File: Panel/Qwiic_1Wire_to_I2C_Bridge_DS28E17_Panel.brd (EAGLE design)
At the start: 45.7 x 27.9 mm, 23 parts, among them J1 RJ45, J2 RJ45, J3 RJ11, J4 RJ11, U1 DS28E17

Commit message: Update to board
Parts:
- removed FRAME1: FRAME-LETTER, SparkFun-Aesthetics:CREATIVE_COMMONS
- added C2: 1.0uF, SparkFun-Capacitors:0603
- added H5, H6, H7, H8: STAND-OFF, SparkFun-Hardware:STAND-OFF
- added J10: (no value), SparkFun-Connectors:1X03
- added J6, J8: RJ45, SparkFun-Connectors:RJ45-8
- added J7, J9: RJ11, SparkFun-Connectors:RJ11-6
- added JP10: (no value), SparkFun-Jumpers:SMT-JUMPER_3_2-NC_PASTE_SILK
- added JP4, JP7: (no value), SparkX:1X04_1MM_RA
- added JP8: (no value), SparkX:1X04
- added JP9: (no value), SparkFun-Jumpers:SMT-JUMPER_2_NC_PASTE_SILK
- added LOGO2: OSHW-LOGOM, SparkFun-Aesthetics:OSHW-LOGO-M
- added R4, R5, R6: 4.7k, SparkFun-Resistors:0603
- added U$1, U$4: SPARKX-LOGO5, SparkX:SPARKX-LARGE
- added U2: DS28E17, SparkX:TQFN-16
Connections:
- new net 3.3V1: J10.3, J6.6, J7.5, J8.6, J9.5, JP10.2, JP4.2, JP7.2, JP8.2, JP9.2, U2.6
- new net AWAKE1: U2.12
- new net BUSY1: U2.13
- new net ED1: U2.5
- new net GND1: C2.2, J10.1, J6.4, J7.3, J8.4, J9.3, JP4.1, JP7.1, JP8.1, U2.4, U2.8
- new net IO1: J10.2, J6.5, J7.4, J8.5, J9.4, R6.1, U2.2, U2.3
- new net N$5: C2.1, U2.7
- new net N$6: JP9.1, R6.2
- new net N$7: JP10.1, R5.2
- new net N$8: JP10.3, R4.2
- new net SCL1: JP4.4, JP7.4, JP8.4, R4.1, U2.15
- new net SDA1: JP4.3, JP7.3, JP8.3, R5.1, U2.16
- new net XD1: U2.14
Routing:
- net 3.3V1: track 0.00 -> 82.0 mm, vias 0 -> 1
- net IO1: track 0.00 -> 48.5 mm
- net SCL1: track 0.00 -> 37.8 mm, vias 0 -> 3
- net SDA1: track 0.00 -> 36.5 mm, vias 0 -> 3
- net N$5: track 0.00 -> 3.68 mm
- net N$6: track 0.00 -> 3.11 mm
- net N$8: track 0.00 -> 2.56 mm
- net N$7: track 0.00 -> 2.56 mm
- added copper zone on layer 1, net GND1
- added copper zone on layer 16, net GND1
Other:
- board size 45.7 x 27.9 mm -> 91.9 x 27.9 mm
- board text removed: "Joel Bartlett"

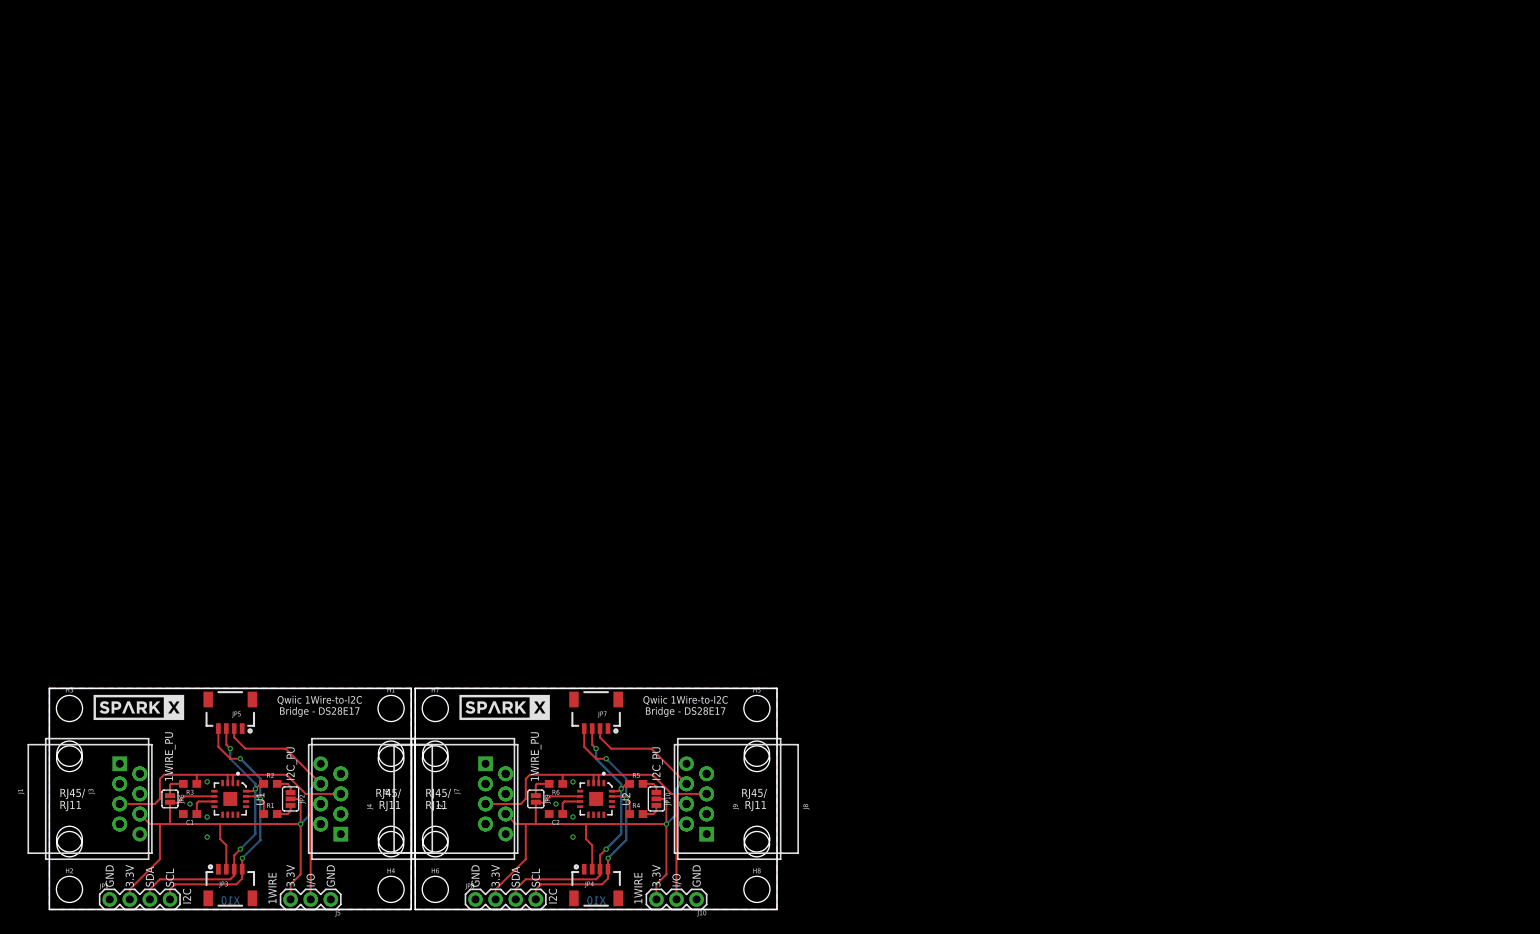
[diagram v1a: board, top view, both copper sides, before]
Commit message: Added RJ45/RJ11 footprint. CAM new panel gerbers
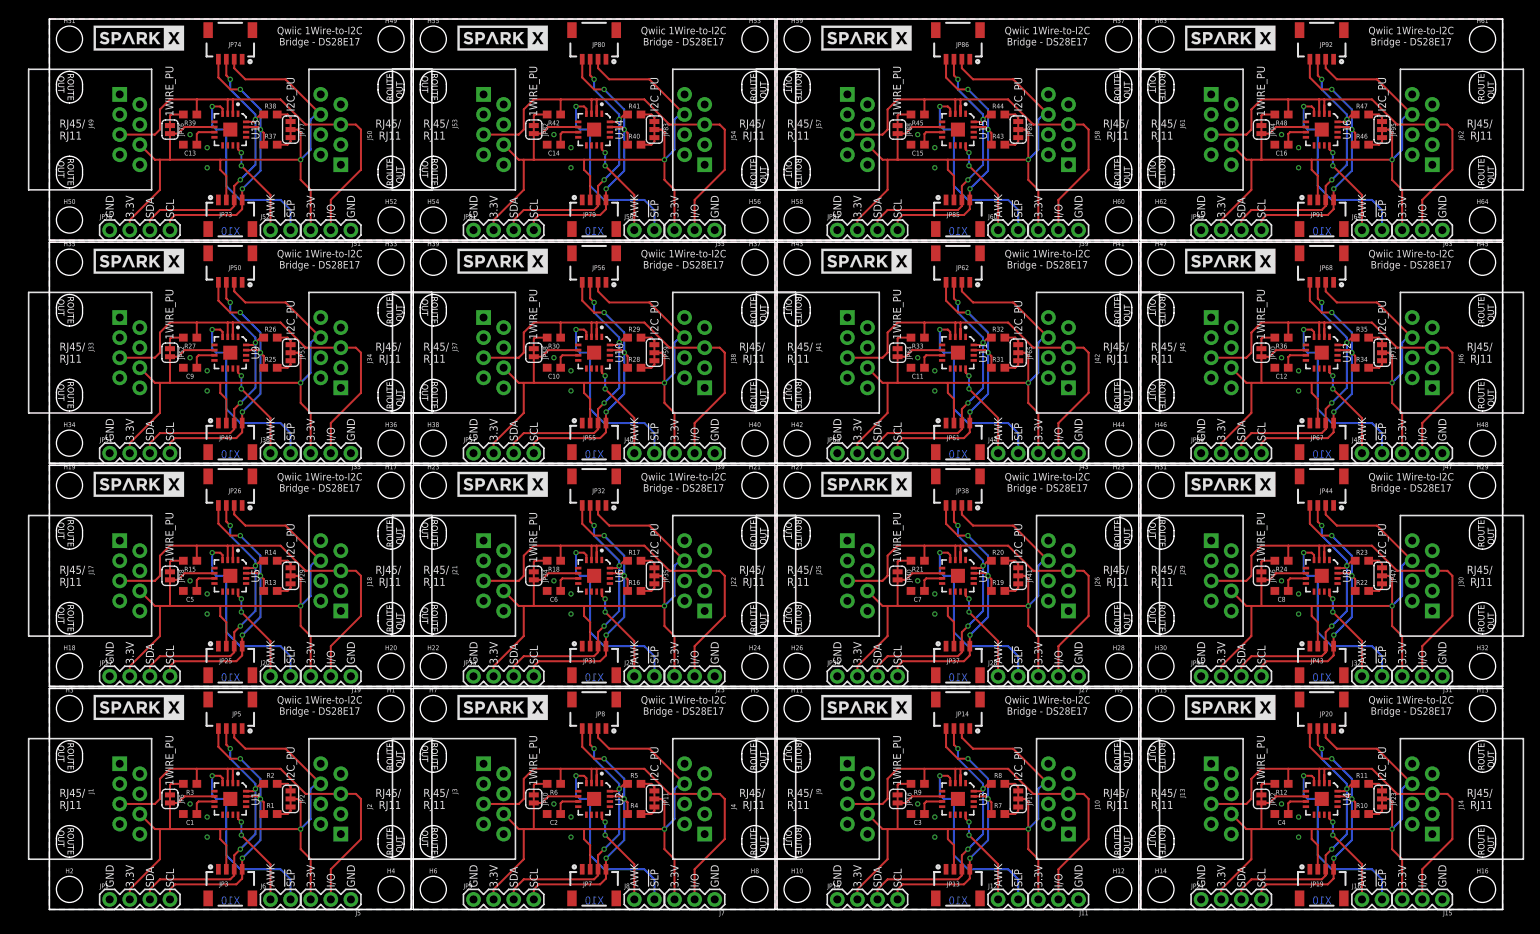
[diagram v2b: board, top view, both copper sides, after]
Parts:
- added C10, C11, C12, C13, C14, C15, C16, C3, C4, C5, C6, C7, C8, C9: 1.0uF, SparkFun-Capacitors:0603
- added FRAME1: FRAME-LETTER, SparkFun-Aesthetics:CREATIVE_COMMONS
- added H10, H11, H12, H13, H14, H15, H16, H17, H18, H19, H20, H21, H22, H23, H24, H25, H26, H27, H28, H29, H30, H31, H32, H33, H34, H35, H36, H37, H38, H39, H40, H41, H42, H43, H44, H45, H46, H47, H48, H49, H50, H51, H52, H53, H54, H55, H56, H57, H58, H59, H60, H61, H62, H63, H64, H9: STAND-OFF, SparkFun-Hardware:STAND-OFF
- added J11, J15, J19, J23, J27, J31, J35, J39, J43, J47, J51, J55, J59, J63: (no value), SparkFun-Connectors:1X03
- added J12, J16, J20, J24, J28, J32, J36, J40, J44, J48, J52, J56, J60, J64: (no value), SparkFun-Connectors:1X02
- added J13, J14, J17, J18, J21, J22, J25, J26, J29, J30, J33, J34, J37, J38, J41, J42, J45, J46, J49, J50, J53, J54, J57, J58, J61, J62: RJ45_RJ11_COMBO, SparkX:RJ45_RJ11_COMBO
- added JP11, JP17, JP23, JP29, JP35, JP41, JP47, JP53, JP59, JP65, JP71, JP77, JP83, JP89, JP95: (no value), SparkFun-Jumpers:SMT-JUMPER_3_2-NC_TRACE_SILK
- added JP12, JP16, JP18, JP22, JP24, JP28, JP30, JP34, JP36, JP40, JP42, JP46, JP48, JP52, JP54, JP58, JP60, JP64, JP66, JP70, JP72, JP76, JP78, JP82, JP84, JP88, JP90, JP94, JP96: (no value), SparkFun-Jumpers:SMT-JUMPER_2_NC_TRACE_SILK
- added JP13, JP14, JP19, JP20, JP25, JP26, JP31, JP32, JP37, JP38, JP43, JP44, JP49, JP50, JP55, JP56, JP61, JP62, JP67, JP68, JP73, JP74, JP79, JP80, JP85, JP86, JP91, JP92: (no value), SparkX:1X04_1MM_RA
- added JP15, JP21, JP27, JP33, JP39, JP45, JP51, JP57, JP63, JP69, JP75, JP81, JP87, JP93: (no value), SparkX:1X04
- added LOGO10, LOGO11, LOGO12, LOGO13, LOGO14, LOGO15, LOGO16, LOGO3, LOGO4, LOGO5, LOGO6, LOGO7, LOGO8, LOGO9: OSHW-LOGOM, SparkFun-Aesthetics:OSHW-LOGO-M
- added R10, R11, R12, R13, R14, R15, R16, R17, R18, R19, R20, R21, R22, R23, R24, R25, R26, R27, R28, R29, R30, R31, R32, R33, R34, R35, R36, R37, R38, R39, R40, R41, R42, R43, R44, R45, R46, R47, R48, R7, R8, R9: 4.7k, SparkFun-Resistors:0603
- added U$10, U$11, U$12, U$13, U$14, U$15, U$16, U$17, U$18, U$19, U$20, U$21, U$22, U$23, U$24, U$25, U$26, U$27, U$28, U$29, U$30, U$31, U$32, U$5, U$6, U$7, U$8, U$9: SPARKX-LOGO5, SparkX:SPARKX-LARGE
- added U10, U11, U12, U13, U14, U15, U16, U3, U4, U5, U6, U7, U8, U9: DS28E17, SparkX:TQFN-16
- J1, J2: value RJ45 -> RJ45_RJ11_COMBO; device SparkFun-Connectors:RJ45-8 -> SparkX:RJ45_RJ11_COMBO
- J10: value (none) -> RJ45_RJ11_COMBO; device SparkFun-Connectors:1X03 -> SparkX:RJ45_RJ11_COMBO
- J3, J4, J9: value RJ11 -> RJ45_RJ11_COMBO; device SparkFun-Connectors:RJ11-6 -> SparkX:RJ45_RJ11_COMBO
- J6, J8: value RJ45 -> (none); device SparkFun-Connectors:RJ45-8 -> SparkFun-Connectors:1X02
- J7: value RJ11 -> (none); device SparkFun-Connectors:RJ11-6 -> SparkFun-Connectors:1X03
- JP10: device SparkFun-Jumpers:SMT-JUMPER_3_2-NC_PASTE_SILK -> SparkFun-Jumpers:SMT-JUMPER_2_NC_TRACE_SILK
- JP2: device SparkFun-Jumpers:SMT-JUMPER_3_2-NC_PASTE_SILK -> SparkFun-Jumpers:SMT-JUMPER_3_2-NC_TRACE_SILK
- JP4: device SparkX:1X04_1MM_RA -> SparkFun-Jumpers:SMT-JUMPER_2_NC_TRACE_SILK
- JP6: device SparkFun-Jumpers:SMT-JUMPER_2_NC_PASTE_SILK -> SparkFun-Jumpers:SMT-JUMPER_2_NC_TRACE_SILK
- JP8: device SparkX:1X04 -> SparkX:1X04_1MM_RA
- JP9: device SparkFun-Jumpers:SMT-JUMPER_2_NC_PASTE_SILK -> SparkX:1X04
- moved J10 54.8 mm to (135.1, 14.0), turned to 90 degrees
- moved JP4 47.1 mm to (22.9, 14.0), flipped to the bottom, turned to 180 degrees
- moved J3 46.0 mm to (48.5, 14.0)
- moved J4 46.0 mm to (89.2, 14.0)
- moved J7 37.5 mm to (84.1, 1.27), turned to 180 degrees
- moved JP8 26.3 mm to (68.8, 22.9), turned to 180 degrees
- moved J6 24.4 mm to (27.9, 1.27), turned to 0 degrees
- moved J8 20.0 mm to (73.9, 1.27), turned to 0 degrees
- moved JP7 17.8 mm to (68.8, 5.08), turned to 0 degrees
- moved JP10 15.5 mm to (61.2, 14.0)
- moved JP9 14.9 mm to (53.6, 1.27), turned to 0 degrees
- moved LOGO2 10.2 mm to (68.8, 3.81)
- moved LOGO1 10.2 mm to (22.9, 3.81)
- moved J9 5.08 mm to (94.5, 14.0), turned to 270 degrees
- moved J5 2.54 mm to (38.1, 1.27)
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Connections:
- new net !SLEEP: J6.2, JP4.1, U1.4
- new net !SLEEP1: J8.2, JP12.1, U2.4
- new net !SLEEP10: J44.2, JP66.1, U11.4
- new net !SLEEP11: J48.2, JP72.1, U12.4
- new net !SLEEP12: J52.2, JP78.1, U13.4
- new net !SLEEP13: J56.2, JP84.1, U14.4
- new net !SLEEP14: J60.2, JP90.1, U15.4
- new net !SLEEP15: J64.2, JP96.1, U16.4
- new net !SLEEP2: J12.2, JP18.1, U3.4
- new net !SLEEP3: J16.2, JP24.1, U4.4
- new net !SLEEP4: J20.2, JP30.1, U5.4
- new net !SLEEP5: J24.2, JP36.1, U6.4
- new net !SLEEP6: J28.2, JP42.1, U7.4
- new net !SLEEP7: J32.2, JP48.1, U8.4
- new net !SLEEP8: J36.2, JP54.1, U9.4
- new net !SLEEP9: J40.2, JP60.1, U10.4
- new net 3.3V10: J41.6, J42.6, J43.3, JP61.2, JP62.2, JP63.2, JP64.2, JP65.2, U11.6
- new net 3.3V11: J45.6, J46.6, J47.3, JP67.2, JP68.2, JP69.2, JP70.2, JP71.2, U12.6
- new net 3.3V12: J49.6, J50.6, J51.3, JP73.2, JP74.2, JP75.2, JP76.2, JP77.2, U13.6
- new net 3.3V13: J53.6, J54.6, J55.3, JP79.2, JP80.2, JP81.2, JP82.2, JP83.2, U14.6
- new net 3.3V14: J57.6, J58.6, J59.3, JP85.2, JP86.2, JP87.2, JP88.2, JP89.2, U15.6
- new net 3.3V15: J61.6, J62.6, J63.3, JP91.2, JP92.2, JP93.2, JP94.2, JP95.2, U16.6
- new net 3.3V2: J10.6, J11.3, J9.6, JP13.2, JP14.2, JP15.2, JP16.2, JP17.2, U3.6
- new net 3.3V3: J13.6, J14.6, J15.3, JP19.2, JP20.2, JP21.2, JP22.2, JP23.2, U4.6
- new net 3.3V4: J17.6, J18.6, J19.3, JP25.2, JP26.2, JP27.2, JP28.2, JP29.2, U5.6
- new net 3.3V5: J21.6, J22.6, J23.3, JP31.2, JP32.2, JP33.2, JP34.2, JP35.2, U6.6
- new net 3.3V6: J25.6, J26.6, J27.3, JP37.2, JP38.2, JP39.2, JP40.2, JP41.2, U7.6
- new net 3.3V7: J29.6, J30.6, J31.3, JP43.2, JP44.2, JP45.2, JP46.2, JP47.2, U8.6
- new net 3.3V8: J33.6, J34.6, J35.3, JP49.2, JP50.2, JP51.2, JP52.2, JP53.2, U9.6
- new net 3.3V9: J37.6, J38.6, J39.3, JP55.2, JP56.2, JP57.2, JP58.2, JP59.2, U10.6
- new net AWAKE10: J44.1, U11.12
- new net AWAKE11: J48.1, U12.12
- new net AWAKE12: J52.1, U13.12
- new net AWAKE13: J56.1, U14.12
- new net AWAKE14: J60.1, U15.12
- new net AWAKE15: J64.1, U16.12
- new net AWAKE2: J12.1, U3.12
- new net AWAKE3: J16.1, U4.12
- new net AWAKE4: J20.1, U5.12
- new net AWAKE5: J24.1, U6.12
- new net AWAKE6: J28.1, U7.12
- new net AWAKE7: J32.1, U8.12
- new net AWAKE8: J36.1, U9.12
- new net AWAKE9: J40.1, U10.12
- new net BUSY10: U11.13
- new net BUSY11: U12.13
- new net BUSY12: U13.13
- new net BUSY13: U14.13
- new net BUSY14: U15.13
- new net BUSY15: U16.13
- new net BUSY2: U3.13
- new net BUSY3: U4.13
- new net BUSY4: U5.13
- new net BUSY5: U6.13
- new net BUSY6: U7.13
- new net BUSY7: U8.13
- new net BUSY8: U9.13
- new net BUSY9: U10.13
- new net ED10: U11.5
- new net ED11: U12.5
- new net ED12: U13.5
- new net ED13: U14.5
- new net ED14: U15.5
- new net ED15: U16.5
- new net ED2: U3.5
- new net ED3: U4.5
- new net ED4: U5.5
- new net ED5: U6.5
- new net ED6: U7.5
- new net ED7: U8.5
- new net ED8: U9.5
- new net ED9: U10.5
- new net GND10: C11.2, J41.4, J42.4, J43.1, JP61.1, JP62.1, JP63.1, JP66.2, U11.8
- new net GND11: C12.2, J45.4, J46.4, J47.1, JP67.1, JP68.1, JP69.1, JP72.2, U12.8
- new net GND12: C13.2, J49.4, J50.4, J51.1, JP73.1, JP74.1, JP75.1, JP78.2, U13.8
- new net GND13: C14.2, J53.4, J54.4, J55.1, JP79.1, JP80.1, JP81.1, JP84.2, U14.8
- new net GND14: C15.2, J57.4, J58.4, J59.1, JP85.1, JP86.1, JP87.1, JP90.2, U15.8
- new net GND15: C16.2, J61.4, J62.4, J63.1, JP91.1, JP92.1, JP93.1, JP96.2, U16.8
- new net GND2: C3.2, J10.4, J11.1, J9.4, JP13.1, JP14.1, JP15.1, JP18.2, U3.8
- new net GND3: C4.2, J13.4, J14.4, J15.1, JP19.1, JP20.1, JP21.1, JP24.2, U4.8
- new net GND4: C5.2, J17.4, J18.4, J19.1, JP25.1, JP26.1, JP27.1, JP30.2, U5.8
- new net GND5: C6.2, J21.4, J22.4, J23.1, JP31.1, JP32.1, JP33.1, JP36.2, U6.8
- new net GND6: C7.2, J25.4, J26.4, J27.1, JP37.1, JP38.1, JP39.1, JP42.2, U7.8
- new net GND7: C8.2, J29.4, J30.4, J31.1, JP43.1, JP44.1, JP45.1, JP48.2, U8.8
- new net GND8: C9.2, J33.4, J34.4, J35.1, JP49.1, JP50.1, JP51.1, JP54.2, U9.8
- new net GND9: C10.2, J37.4, J38.4, J39.1, JP55.1, JP56.1, JP57.1, JP60.2, U10.8
- new net IO10: J41.5, J42.5, J43.2, R33.1, U11.2, U11.3
- new net IO11: J45.5, J46.5, J47.2, R36.1, U12.2, U12.3
- new net IO12: J49.5, J50.5, J51.2, R39.1, U13.2, U13.3
- new net IO13: J53.5, J54.5, J55.2, R42.1, U14.2, U14.3
- new net IO14: J57.5, J58.5, J59.2, R45.1, U15.2, U15.3
- new net IO15: J61.5, J62.5, J63.2, R48.1, U16.2, U16.3
- new net IO2: J10.5, J11.2, J9.5, R9.1, U3.2, U3.3
- new net IO3: J13.5, J14.5, J15.2, R12.1, U4.2, U4.3
- new net IO4: J17.5, J18.5, J19.2, R15.1, U5.2, U5.3
- new net IO5: J21.5, J22.5, J23.2, R18.1, U6.2, U6.3
- new net IO6: J25.5, J26.5, J27.2, R21.1, U7.2, U7.3
- new net IO7: J29.5, J30.5, J31.2, R24.1, U8.2, U8.3
- new net IO8: J33.5, J34.5, J35.2, R27.1, U9.2, U9.3
- new net IO9: J37.5, J38.5, J39.2, R30.1, U10.2, U10.3
- new net N$10: JP16.1, R9.2
- new net N$11: JP17.1, R8.2
- new net N$12: JP17.3, R7.2
- new net N$13: C4.1, U4.7
- new net N$14: JP22.1, R12.2
- new net N$15: JP23.1, R11.2
- new net N$16: JP23.3, R10.2
- new net N$17: C5.1, U5.7
- new net N$18: JP28.1, R15.2
- new net N$19: JP29.1, R14.2
- new net N$20: JP29.3, R13.2
- new net N$21: C6.1, U6.7
- new net N$22: JP34.1, R18.2
- new net N$23: JP35.1, R17.2
- new net N$24: JP35.3, R16.2
- new net N$25: C7.1, U7.7
- new net N$26: JP40.1, R21.2
- new net N$27: JP41.1, R20.2
- new net N$28: JP41.3, R19.2
- new net N$29: C8.1, U8.7
- new net N$30: JP46.1, R24.2
- new net N$31: JP47.1, R23.2
- new net N$32: JP47.3, R22.2
- new net N$33: C9.1, U9.7
- new net N$34: JP52.1, R27.2
- new net N$35: JP53.1, R26.2
- new net N$36: JP53.3, R25.2
- new net N$37: C10.1, U10.7
- new net N$38: JP58.1, R30.2
- new net N$39: JP59.1, R29.2
- new net N$40: JP59.3, R28.2
- new net N$41: C11.1, U11.7
- new net N$42: JP64.1, R33.2
- new net N$43: JP65.1, R32.2
- new net N$44: JP65.3, R31.2
- new net N$45: C12.1, U12.7
- new net N$46: JP70.1, R36.2
- new net N$47: JP71.1, R35.2
- new net N$48: JP71.3, R34.2
- new net N$49: C13.1, U13.7
- new net N$50: JP76.1, R39.2
- new net N$51: JP77.1, R38.2
- new net N$52: JP77.3, R37.2
- new net N$53: C14.1, U14.7
- new net N$54: JP82.1, R42.2
- new net N$55: JP83.1, R41.2
- new net N$56: JP83.3, R40.2
- new net N$57: C15.1, U15.7
- new net N$58: JP88.1, R45.2
- new net N$59: JP89.1, R44.2
- new net N$60: JP89.3, R43.2
- new net N$61: C16.1, U16.7
- new net N$62: JP94.1, R48.2
- new net N$63: JP95.1, R47.2
- new net N$64: JP95.3, R46.2
- new net N$9: C3.1, U3.7
- new net SCL10: JP61.4, JP62.4, JP63.4, R31.1, U11.15
- new net SCL11: JP67.4, JP68.4, JP69.4, R34.1, U12.15
- new net SCL12: JP73.4, JP74.4, JP75.4, R37.1, U13.15
- new net SCL13: JP79.4, JP80.4, JP81.4, R40.1, U14.15
- new net SCL14: JP85.4, JP86.4, JP87.4, R43.1, U15.15
- new net SCL15: JP91.4, JP92.4, JP93.4, R46.1, U16.15
- new net SCL2: JP13.4, JP14.4, JP15.4, R7.1, U3.15
- new net SCL3: JP19.4, JP20.4, JP21.4, R10.1, U4.15
- new net SCL4: JP25.4, JP26.4, JP27.4, R13.1, U5.15
- new net SCL5: JP31.4, JP32.4, JP33.4, R16.1, U6.15
- new net SCL6: JP37.4, JP38.4, JP39.4, R19.1, U7.15
- new net SCL7: JP43.4, JP44.4, JP45.4, R22.1, U8.15
- new net SCL8: JP49.4, JP50.4, JP51.4, R25.1, U9.15
- new net SCL9: JP55.4, JP56.4, JP57.4, R28.1, U10.15
- new net SDA10: JP61.3, JP62.3, JP63.3, R32.1, U11.16
- new net SDA11: JP67.3, JP68.3, JP69.3, R35.1, U12.16
- new net SDA12: JP73.3, JP74.3, JP75.3, R38.1, U13.16
- new net SDA13: JP79.3, JP80.3, JP81.3, R41.1, U14.16
- new net SDA14: JP85.3, JP86.3, JP87.3, R44.1, U15.16
- new net SDA15: JP91.3, JP92.3, JP93.3, R47.1, U16.16
- new net SDA2: JP13.3, JP14.3, JP15.3, R8.1, U3.16
- new net SDA3: JP19.3, JP20.3, JP21.3, R11.1, U4.16
- new net SDA4: JP25.3, JP26.3, JP27.3, R14.1, U5.16
- new net SDA5: JP31.3, JP32.3, JP33.3, R17.1, U6.16
- new net SDA6: JP37.3, JP38.3, JP39.3, R20.1, U7.16
- new net SDA7: JP43.3, JP44.3, JP45.3, R23.1, U8.16
- new net SDA8: JP49.3, JP50.3, JP51.3, R26.1, U9.16
- new net SDA9: JP55.3, JP56.3, JP57.3, R29.1, U10.16
- new net XD10: U11.14
- new net XD11: U12.14
- new net XD12: U13.14
- new net XD13: U14.14
- new net XD14: U15.14
- new net XD15: U16.14
- new net XD2: U3.14
- new net XD3: U4.14
- new net XD4: U5.14
- new net XD5: U6.14
- new net XD6: U7.14
- new net XD7: U8.14
- new net XD8: U9.14
- new net XD9: U10.14
- net 3.3V: no longer J3.5, J4.5
- net 3.3V1: now also J3.6, J4.6, J7.3, JP11.2; no longer J10.3, J6.6, J7.5, J8.6, J9.5, JP4.2
- net AWAKE: now also J6.1
- net AWAKE1: now also J8.1
- net GND: now also JP4.2; no longer J3.3, J4.3, U1.4
- net GND1: now also J3.4, J4.4, J7.1, JP12.2, JP9.1; no longer J10.1, J6.4, J7.3, J8.4, J9.3, JP4.1, U2.4
- net IO: no longer J3.4, J4.4
- net IO1: now also J3.5, J4.5, J7.2; no longer J10.2, J6.5, J7.4, J8.5, J9.4
- net N$6: now also JP10.1; no longer JP9.1
- net N$7: now also JP11.1; no longer JP10.1
- net N$8: now also JP11.3; no longer JP10.3
- net SCL1: now also JP9.4; no longer JP4.4
- net SDA1: now also JP9.3; no longer JP4.3
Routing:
- net 3.3V2: track 0.00 -> 82.1 mm, vias 0 -> 1
- net 3.3V10: track 0.00 -> 82.1 mm, vias 0 -> 1
- net 3.3V6: track 0.00 -> 82.1 mm, vias 0 -> 1
- net 3.3V4: track 0.00 -> 82.1 mm, vias 0 -> 1
- net 3.3V11: track 0.00 -> 82.1 mm, vias 0 -> 1
- net 3.3V9: track 0.00 -> 82.1 mm, vias 0 -> 1
- net 3.3V3: track 0.00 -> 82.1 mm, vias 0 -> 1
- net 3.3V14: track 0.00 -> 82.1 mm, vias 0 -> 1
- net 3.3V8: track 0.00 -> 82.1 mm, vias 0 -> 1
- net 3.3V7: track 0.00 -> 82.1 mm, vias 0 -> 1
- net 3.3V5: track 0.00 -> 82.1 mm, vias 0 -> 1
- net 3.3V15: track 0.00 -> 82.1 mm, vias 0 -> 1
- net 3.3V13: track 0.00 -> 82.1 mm, vias 0 -> 1
- net 3.3V12: track 0.00 -> 82.1 mm, vias 0 -> 1
- net IO10: track 0.00 -> 56.2 mm
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- added copper zone on layer 1, net GND10
- added copper zone on layer 16, net GND10
- added copper zone on layer 1, net GND11
- added copper zone on layer 16, net GND11
- added copper zone on layer 1, net GND12
- added copper zone on layer 16, net GND12
- added copper zone on layer 1, net GND13
- added copper zone on layer 16, net GND13
- added copper zone on layer 1, net GND14
- added copper zone on layer 16, net GND14
- added copper zone on layer 1, net GND15
- added copper zone on layer 16, net GND15
- added copper zone on layer 1, net GND2
- added copper zone on layer 16, net GND2
- added copper zone on layer 1, net GND3
- added copper zone on layer 16, net GND3
- added copper zone on layer 1, net GND4
- added copper zone on layer 16, net GND4
- added copper zone on layer 1, net GND5
- added copper zone on layer 16, net GND5
- added copper zone on layer 1, net GND6
- added copper zone on layer 16, net GND6
- added copper zone on layer 1, net GND7
- added copper zone on layer 16, net GND7
- added copper zone on layer 1, net GND8
- added copper zone on layer 16, net GND8
- added copper zone on layer 1, net GND9
- added copper zone on layer 16, net GND9
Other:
- board size 91.9 x 27.9 mm -> 183.6 x 112.5 mm
- board text added: "!SLP"
- board text added: "AWK"
- board text added: "Joel Bartlett"
- board text added: "SLEEP"
